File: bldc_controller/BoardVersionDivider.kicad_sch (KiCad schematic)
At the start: 2 parts

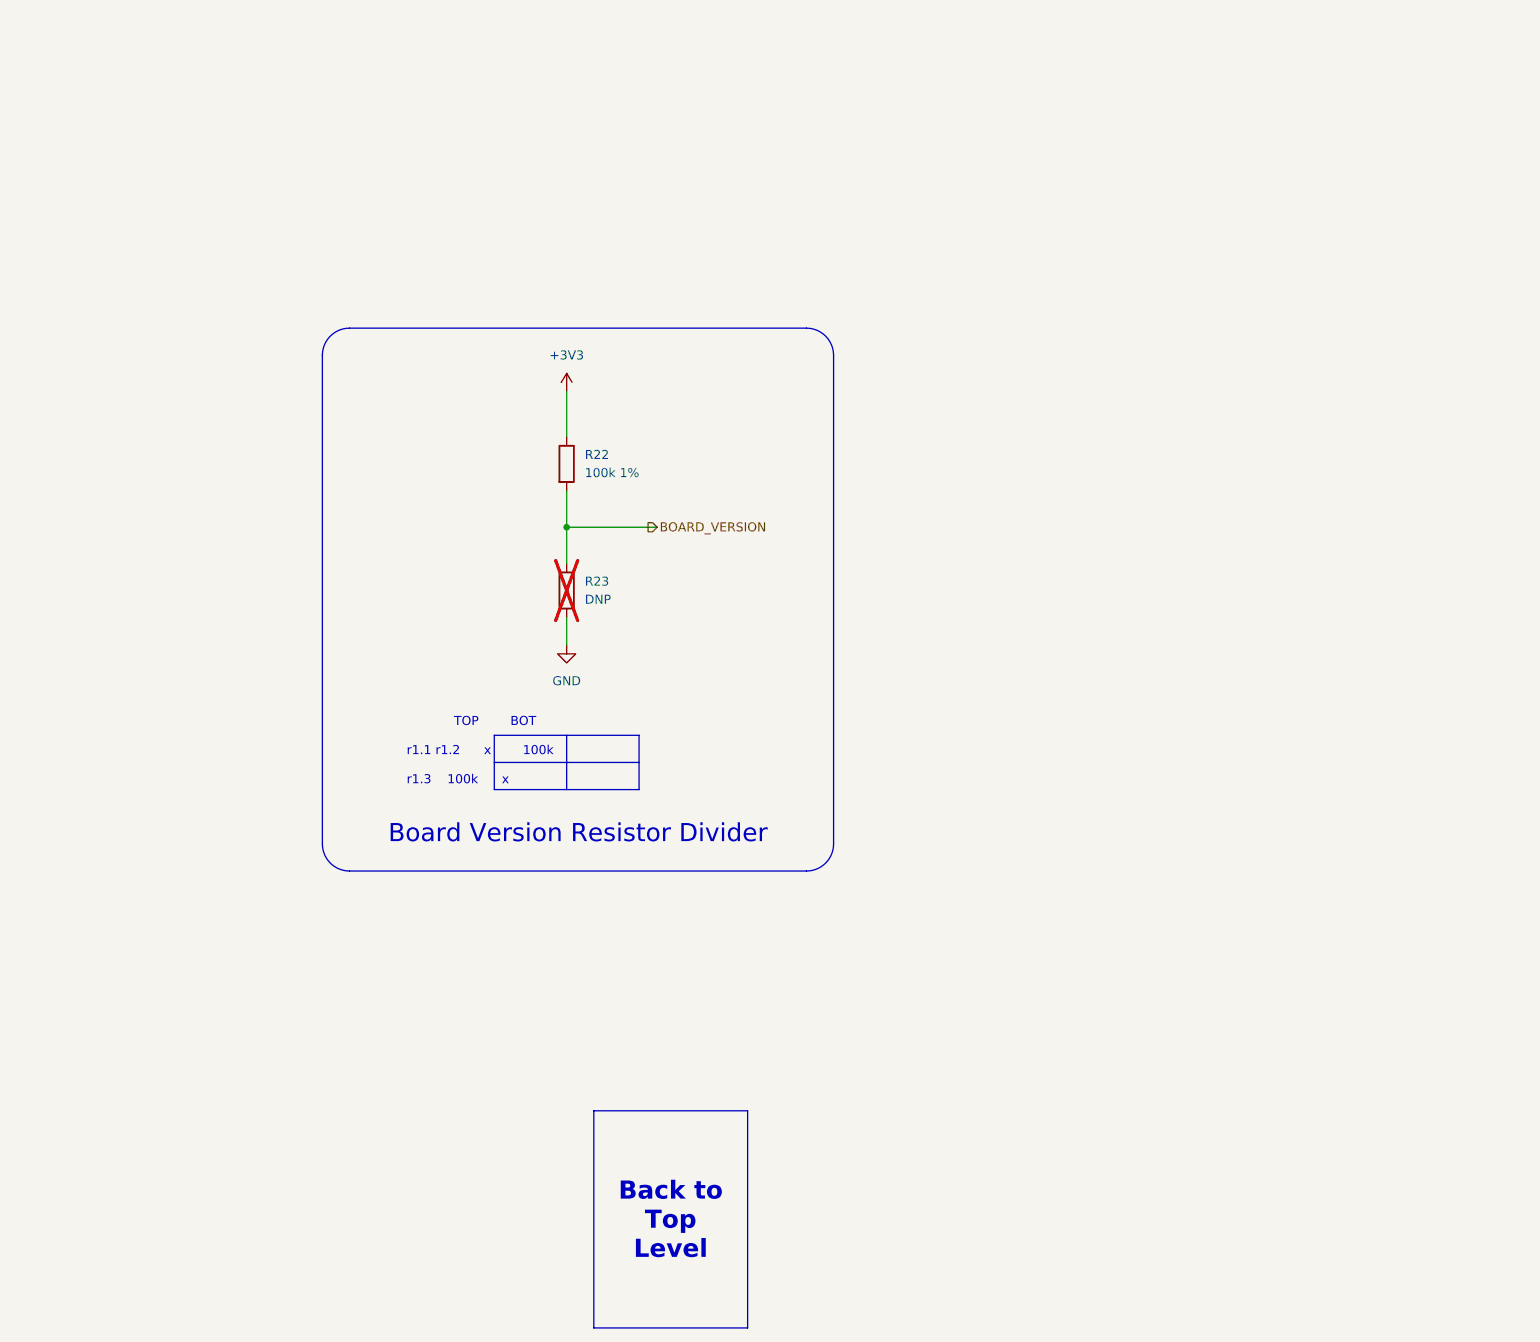
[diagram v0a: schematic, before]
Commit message: added temporary footprints and deleted extra files
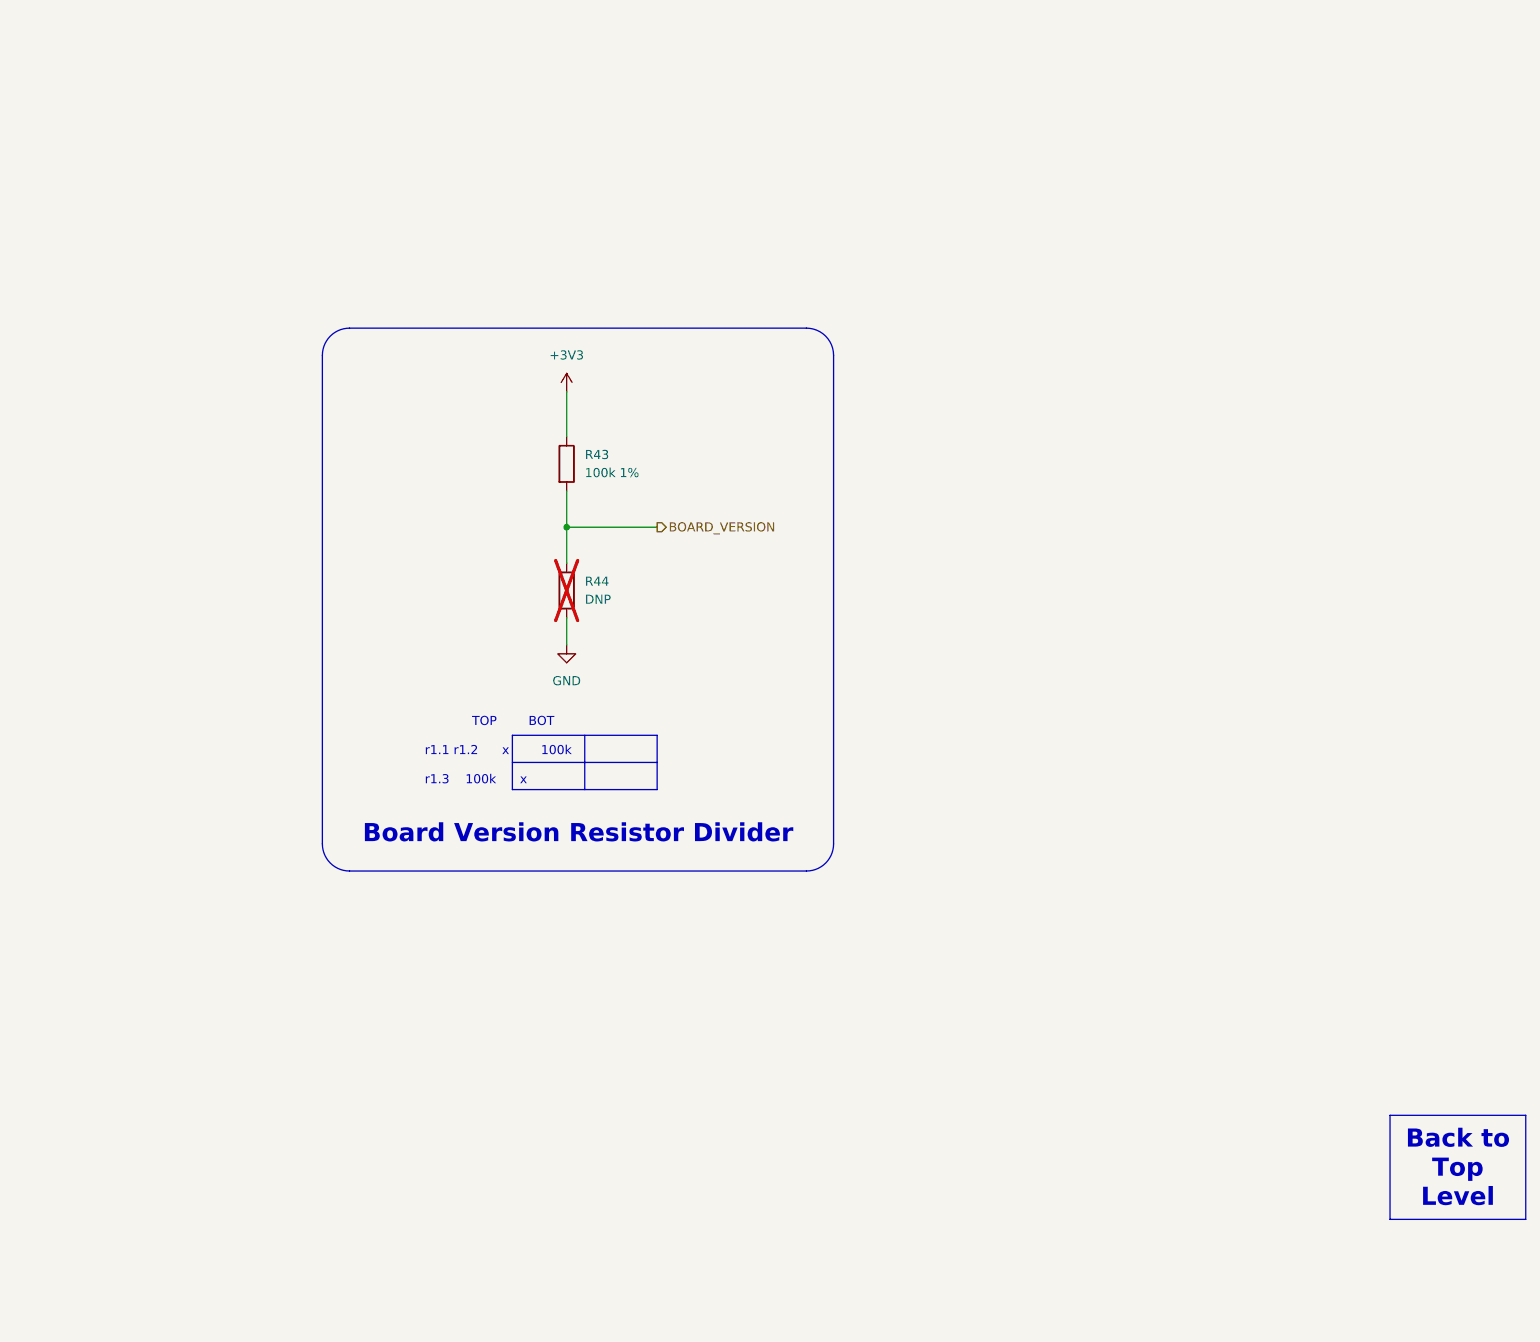
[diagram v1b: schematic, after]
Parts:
- R43: renamed from R22; footprint (none) -> Resistor_SMD:R_0402_1005Metric
- R44: renamed from R23; footprint (none) -> Resistor_SMD:R_0402_1005Metric
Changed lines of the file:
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@@
     (stroke (width 0) (type default))
   )
-  (polyline (pts (xy 149.86 113.03) (xy 149.86 120.65))
+  (polyline (pts (xy 152.4 113.03) (xy 152.4 120.65))
     (stroke (width 0) (type default))
   )
@@
     (stroke (width 0) (type default))
   )
-  (polyline (pts (xy 139.7 116.84) (xy 160.02 116.84))
+  (polyline (pts (xy 142.24 116.84) (xy 162.56 116.84))
     (stroke (width 0) (type default))
   )
@@
     (fill (type none))
   )
-  (rectangle (start 139.7 113.03) (end 160.02 120.65)
+  (rectangle (start 142.24 113.03) (end 162.56 120.65)
     (stroke (width 0) (type default))
     (fill (type none))
@@
     (fill (type none))
   )
+  (text_box "			TOP		BOT\n\nr1.1 r1.2	  x		100k\n\n     r1.3	100k	  x"
+    (at 128.905 109.22 0) (size 33.02 8.89)
+    (stroke (width -0.0001) (type default))
+    (fill (type none))
+    (effects (font (size 1.27 1.27)) (justify left top))
+  )
   (text_box "Back to Top Level"
-    (at 153.67 165.735 0) (size 21.59 30.48)
+    (at 265.43 166.37 0) (size 19.05 14.605)
     (stroke (width 0) (type default) (color 0 0 0 1))
     (fill (type color) (color 0 0 0 0.1))
     (effects (font (size 2.54 2.54) (thickness 0.508) bold (color 0 0 0 1)) (href "#1"))
-  )
-  (text_box "			TOP		BOT\n\nr1.1 r1.2	  x		100k\n\n     r1.3	100k	  x"
-    (at 126.365 109.22 0) (size 33.02 8.89)
-    (stroke (width -0.0001) (type default))
-    (fill (type none))
-    (effects (font (size 1.27 1.27)) (justify left top))
   )
   (text_box "Board Version Resistor Divider"
@@
     (stroke (width -0.0001) (type default))
     (fill (type none))
-    (effects (font (size 2.54 2.54) (color 0 0 0 1)) (justify bottom))
+    (effects (font (size 2.54 2.54) (thickness 0.508) bold (color 0 0 0 1)) (justify bottom))
   )
-  (hierarchical_label "BOARD_VERSION" (shape output) (at 161.29 83.82 0) (fields_autoplaced)
+  (hierarchical_label "BOARD_VERSION" (shape output) (at 162.56 83.82 0) (fields_autoplaced)
     (effects (font (size 1.27 1.27)) (justify left))
   )
   (symbol (lib_id "Device:R") (at 149.86 92.71 0) (unit 1)
     (in_bom no) (on_board yes) (dnp yes) (fields_autoplaced)
-    (property "Reference" "R23" (at 152.4 91.44 0)
+    (property "Reference" "R44" (at 152.4 91.44 0)
       (effects (font (size 1.27 1.27)) (justify left))
     )
@@
       (effects (font (size 1.27 1.27)) (justify left))
     )
-    (property "Footprint" "" (at 148.082 92.71 90)
+    (property "Footprint" "Resistor_SMD:R_0402_1005Metric" (at 148.082 92.71 90)
       (effects (font (size 1.27 1.27)) hide)
     )
@@
       (project "bldc_controller"
         (path "/0650c7a8-acba-429c-9f8e-eec0baf0bc1c/6ac64cfc-cd02-4504-88c7-a17dadca0833"
-          (reference "R23") (unit 1)
+          (reference "R44") (unit 1)
         )
       )
@@
   (symbol (lib_id "power:+3V3") (at 149.86 64.77 0) (unit 1)
     (in_bom yes) (on_board yes) (dnp no) (fields_autoplaced)
-    (property "Reference" "#PWR039" (at 149.86 68.58 0)
+    (property "Reference" "#PWR071" (at 149.86 68.58 0)
       (effects (font (size 1.27 1.27)) hide)
     )
@@
       (project "bldc_controller"
         (path "/0650c7a8-acba-429c-9f8e-eec0baf0bc1c/6ac64cfc-cd02-4504-88c7-a17dadca0833"
-          (reference "#PWR039") (unit 1)
+          (reference "#PWR071") (unit 1)
         )
       )
@@
   (symbol (lib_id "power:GND") (at 149.86 100.33 0) (unit 1)
     (in_bom yes) (on_board yes) (dnp no) (fields_autoplaced)
-    (property "Reference" "#PWR038" (at 149.86 106.68 0)
+    (property "Reference" "#PWR072" (at 149.86 106.68 0)
       (effects (font (size 1.27 1.27)) hide)
     )
@@
       (project "bldc_controller"
         (path "/0650c7a8-acba-429c-9f8e-eec0baf0bc1c/6ac64cfc-cd02-4504-88c7-a17dadca0833"
-          (reference "#PWR038") (unit 1)
+          (reference "#PWR072") (unit 1)
         )
       )
@@
   (symbol (lib_id "Device:R") (at 149.86 74.93 0) (unit 1)
     (in_bom yes) (on_board yes) (dnp no) (fields_autoplaced)
-    (property "Reference" "R22" (at 152.4 73.66 0)
+    (property "Reference" "R43" (at 152.4 73.66 0)
       (effects (font (size 1.27 1.27)) (justify left))
     )
@@
       (effects (font (size 1.27 1.27)) (justify left))
     )
-    (property "Footprint" "" (at 148.082 74.93 90)
+    (property "Footprint" "Resistor_SMD:R_0402_1005Metric" (at 148.082 74.93 90)
       (effects (font (size 1.27 1.27)) hide)
     )
@@
       (project "bldc_controller"
         (path "/0650c7a8-acba-429c-9f8e-eec0baf0bc1c/6ac64cfc-cd02-4504-88c7-a17dadca0833"
-          (reference "R22") (unit 1)
+          (reference "R43") (unit 1)
         )
       )

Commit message: added IPC-7351 compliant footprints and started routing
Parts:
- R43, R44: footprint Resistor_SMD:R_0402_1005Metric -> 0_resistor_smd:R_0402_1005_DensityHigh
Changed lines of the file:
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@@
       (effects (font (size 1.27 1.27)) (justify left))
     )
-    (property "Footprint" "Resistor_SMD:R_0402_1005Metric" (at 148.082 92.71 90)
+    (property "Footprint" "0_resistor_smd:R_0402_1005_DensityHigh" (at 148.082 92.71 90)
       (effects (font (size 1.27 1.27)) hide)
     )
@@
   (symbol (lib_id "power:+3V3") (at 149.86 64.77 0) (unit 1)
     (in_bom yes) (on_board yes) (dnp no) (fields_autoplaced)
-    (property "Reference" "#PWR071" (at 149.86 68.58 0)
+    (property "Reference" "#PWR070" (at 149.86 68.58 0)
       (effects (font (size 1.27 1.27)) hide)
     )
@@
       (project "bldc_controller"
         (path "/0650c7a8-acba-429c-9f8e-eec0baf0bc1c/6ac64cfc-cd02-4504-88c7-a17dadca0833"
-          (reference "#PWR071") (unit 1)
+          (reference "#PWR070") (unit 1)
         )
       )
@@
   (symbol (lib_id "power:GND") (at 149.86 100.33 0) (unit 1)
     (in_bom yes) (on_board yes) (dnp no) (fields_autoplaced)
-    (property "Reference" "#PWR072" (at 149.86 106.68 0)
+    (property "Reference" "#PWR071" (at 149.86 106.68 0)
       (effects (font (size 1.27 1.27)) hide)
     )
@@
       (project "bldc_controller"
         (path "/0650c7a8-acba-429c-9f8e-eec0baf0bc1c/6ac64cfc-cd02-4504-88c7-a17dadca0833"
-          (reference "#PWR072") (unit 1)
+          (reference "#PWR071") (unit 1)
         )
       )
@@
       (effects (font (size 1.27 1.27)) (justify left))
     )
-    (property "Footprint" "Resistor_SMD:R_0402_1005Metric" (at 148.082 74.93 90)
+    (property "Footprint" "0_resistor_smd:R_0402_1005_DensityHigh" (at 148.082 74.93 90)
       (effects (font (size 1.27 1.27)) hide)
     )

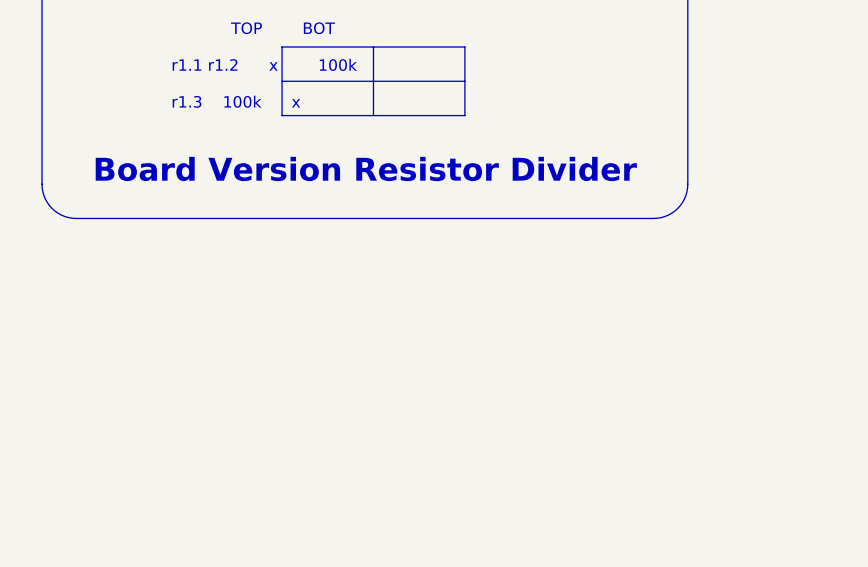
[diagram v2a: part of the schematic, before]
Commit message: Added TVS diodes to all interfaces
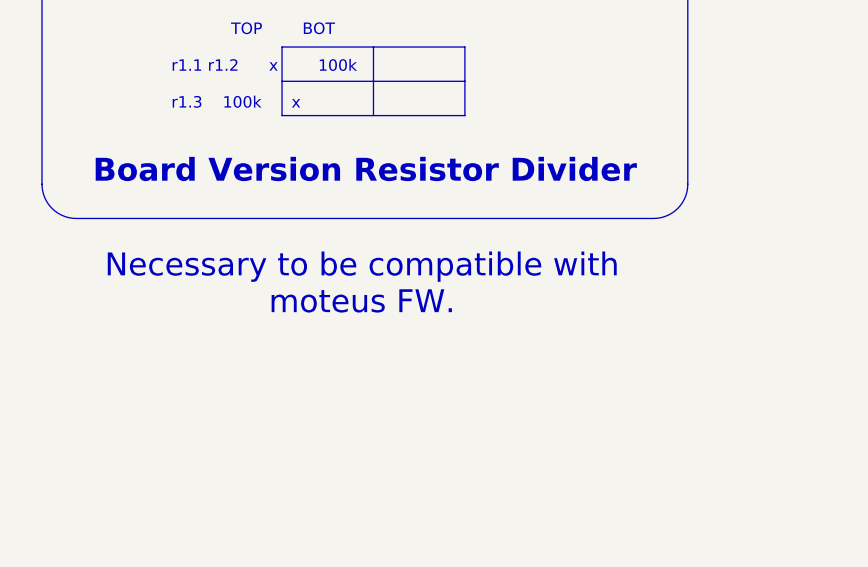
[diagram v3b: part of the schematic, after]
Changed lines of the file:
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@@
     (fill (type none))
+  )
+  (text_box "Necessary to be compatible with moteus FW."
+    (at 115.57 133.35 0) (size 71.12 11.43)
+    (stroke (width -0.0001) (type default))
+    (fill (type none))
+    (effects (font (size 2.54 2.54) (color 0 0 0 1)) (justify bottom))
   )
   (text_box "			TOP		BOT\n\nr1.1 r1.2	  x		100k\n\n     r1.3	100k	  x"
